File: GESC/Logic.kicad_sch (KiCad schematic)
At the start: 45 parts, among them J10 BOOT0, J11 NRST, J12 TYPE-C-31-M-12, J13 Conn_01x07, J9 STLINK, U4 STM32F405RGTx, Y1 8MHz

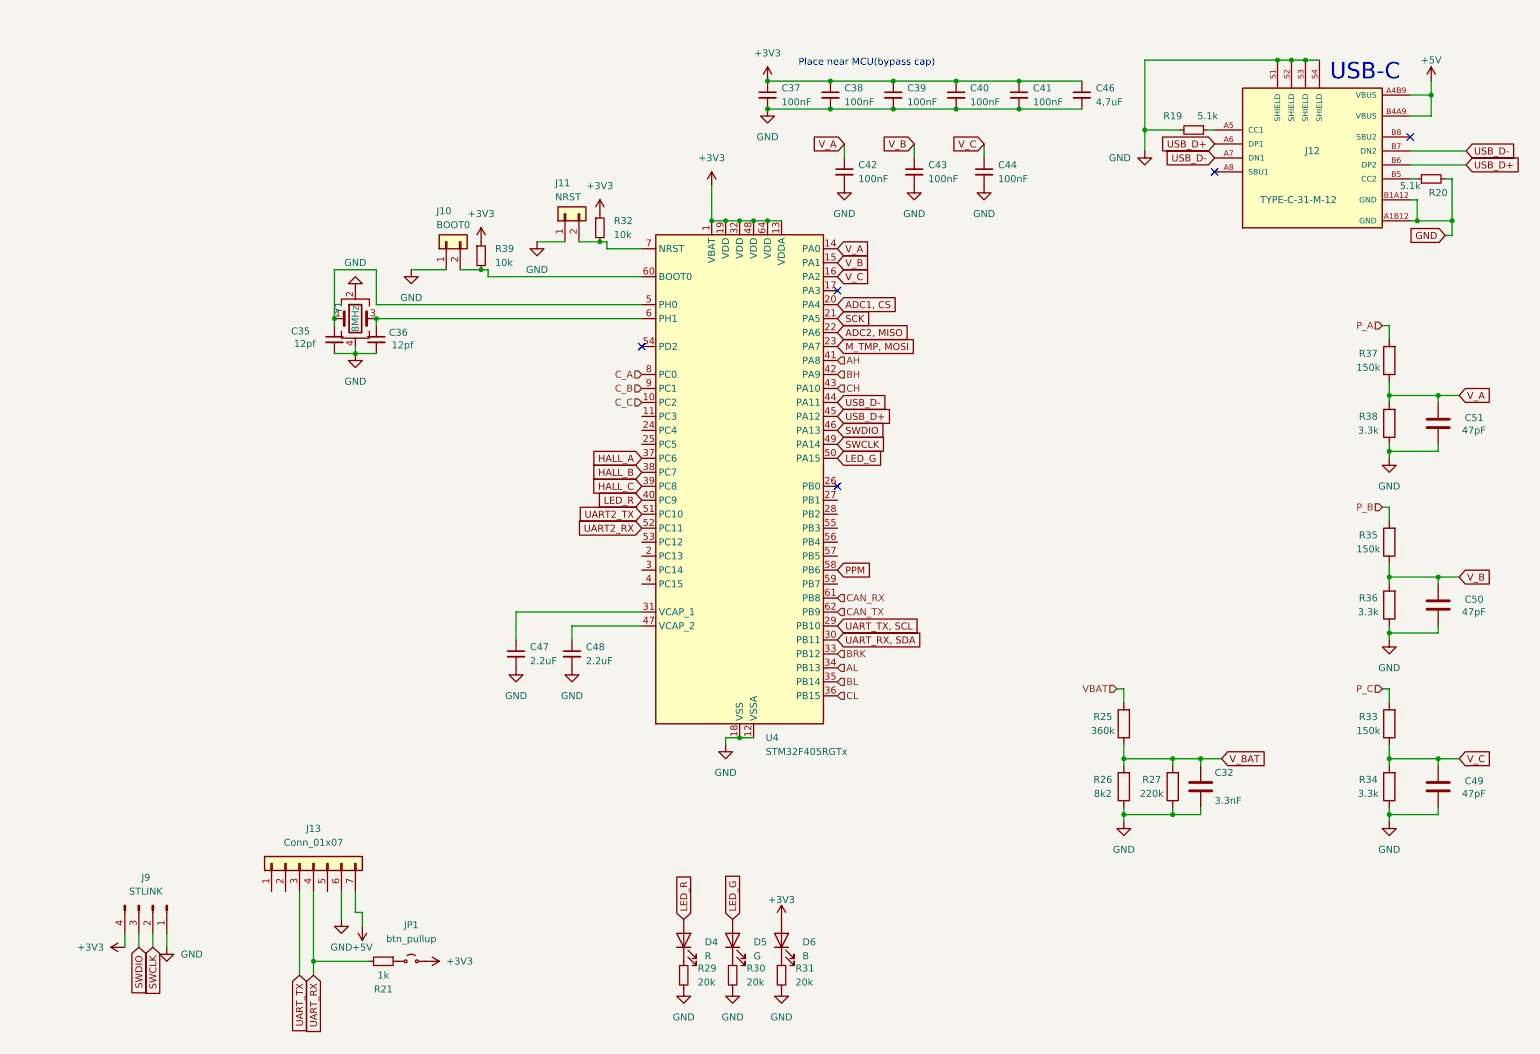
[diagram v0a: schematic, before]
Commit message: ninebot style conn
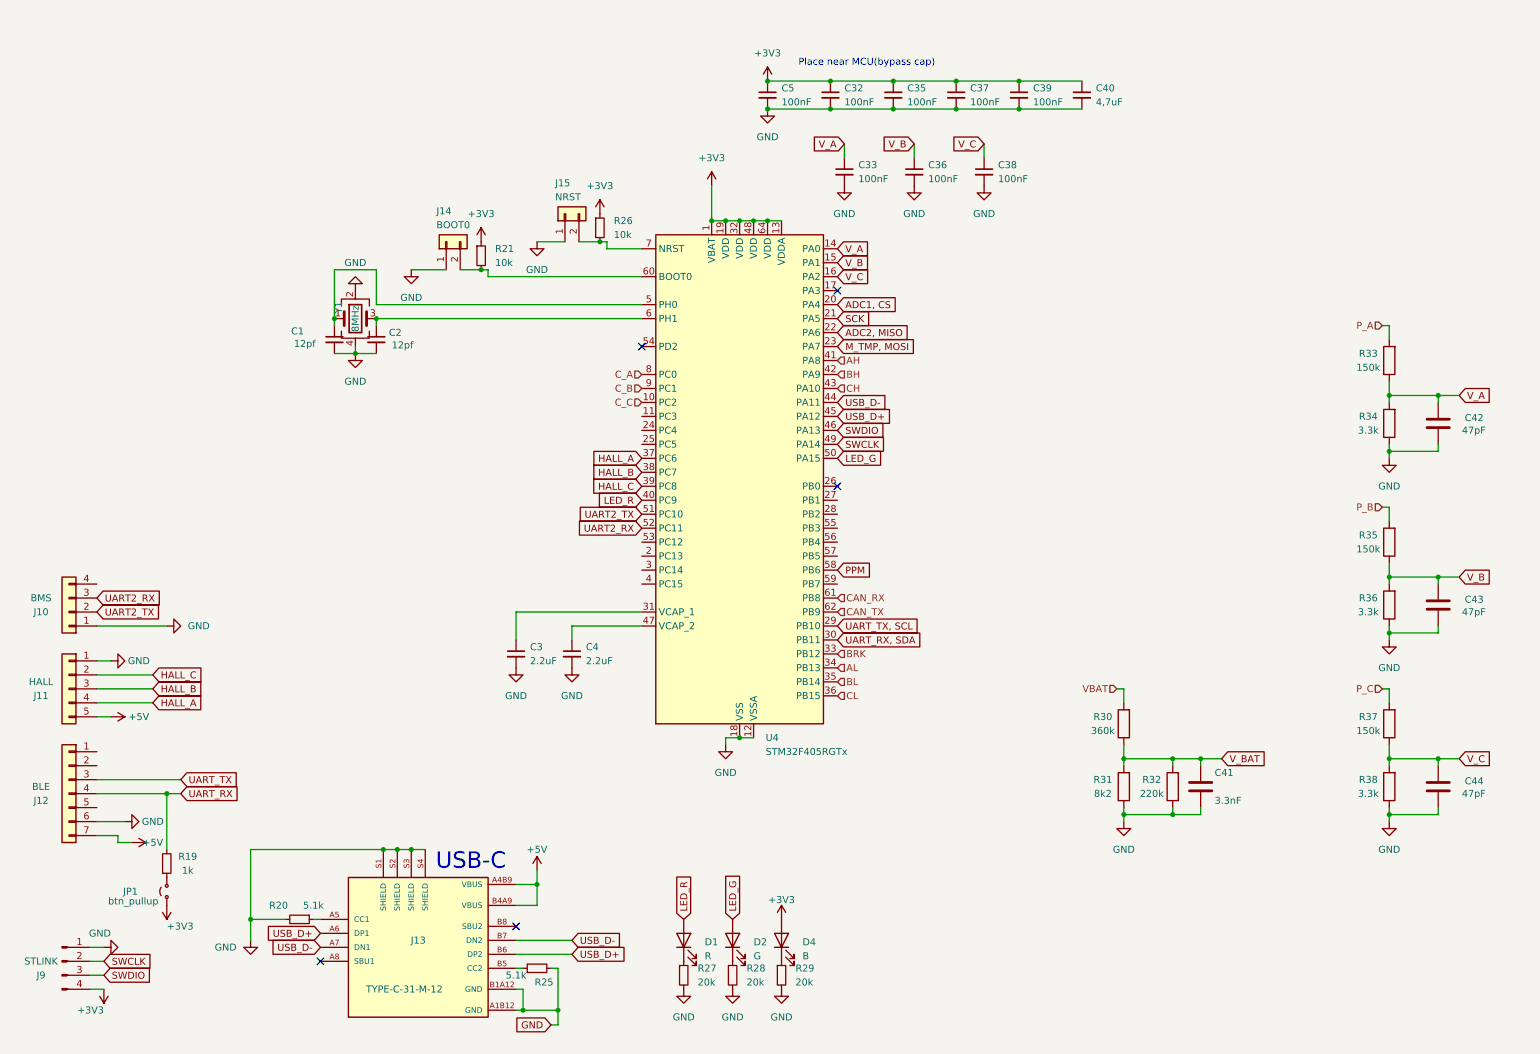
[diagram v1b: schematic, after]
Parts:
- removed C32: 3.3nF, Capacitor_SMD:C_0603_1608Metric, symbol Device:C
- removed C41, C42, C43, C44: 100nF, symbol Device:C_Small
- removed C46: 4,7uF, symbol Device:C_Small
- removed C47, C48: 2.2uF, symbol Device:C_Small
- removed C49, C50, C51: 47pF, Capacitor_SMD:C_0603_1608Metric, symbol Device:C
- removed D5: G, LED_SMD:LED_0603_1608Metric, symbol Device:LED
- removed D6: B, LED_SMD:LED_0603_1608Metric, symbol Device:LED
- removed J10: BOOT0, symbol Connector_Generic:Conn_01x02
- removed J11: NRST, symbol Connector_Generic:Conn_01x02
- removed J12: TYPE-C-31-M-12, Connector_USB:USB_C_Receptacle_HRO_TYPE-C-31-M-12, symbol TYPE-C-31-M-12:TYPE-C-31-M-12
- removed J13: Conn_01x07, symbol Connector_Generic:Conn_01x07
- removed R25: 360k, Resistor_SMD:R_0805_2012Metric, symbol Device:R
- removed R26: 8k2, Resistor_SMD:R_0603_1608Metric, symbol Device:R
- removed R27: 220k, Resistor_SMD:R_0603_1608Metric, symbol Device:R
- removed R30, R31: 20k, Resistor_SMD:R_0603_1608Metric, symbol Device:R_Small
- removed R32, R39: 10k, symbol Device:R_Small
- added C1, C2: 12pf, Capacitor_SMD:C_0603_1608Metric, symbol Device:C_Small
- added C3, C4: 2.2uF, symbol Device:C_Small
- added C32, C33, C5: 100nF, symbol Device:C_Small
- added C41: 3.3nF, Capacitor_SMD:C_0603_1608Metric, symbol Device:C
- added C42, C43, C44: 47pF, Capacitor_SMD:C_0603_1608Metric, symbol Device:C
- added D1: R, LED_SMD:LED_0603_1608Metric, symbol Device:LED
- added D2: G, LED_SMD:LED_0603_1608Metric, symbol Device:LED
- added J10: BMS, symbol Connector_Generic:Conn_01x04
- added J11: HALL, symbol Connector_Generic:Conn_01x05
- added J12: BLE, symbol Connector_Generic:Conn_01x07
- added J13: TYPE-C-31-M-12, Connector_USB:USB_C_Receptacle_HRO_TYPE-C-31-M-12, symbol TYPE-C-31-M-12:TYPE-C-31-M-12
- added J14: BOOT0, symbol Connector_Generic:Conn_01x02
- added J15: NRST, symbol Connector_Generic:Conn_01x02
- added R25: 5.1k, Resistor_SMD:R_0402_1005Metric, symbol Device:R_Small
- added R26: 10k, symbol Device:R_Small
- added R27, R28: 20k, Resistor_SMD:R_0603_1608Metric, symbol Device:R_Small
- added R30: 360k, Resistor_SMD:R_0805_2012Metric, symbol Device:R
- added R31: 8k2, Resistor_SMD:R_0603_1608Metric, symbol Device:R
- added R32: 220k, Resistor_SMD:R_0603_1608Metric, symbol Device:R
- C35, C36: value 12pf -> 100nF; footprint Capacitor_SMD:C_0603_1608Metric -> (none); LCSC C519482 -> (none)
- C40: value 100nF -> 4,7uF
- D4: value R -> B; LCSC C2286 -> C2689219
- R19: value 5.1k -> 1k; footprint Resistor_SMD:R_0402_1005Metric -> (none); LCSC C105872 -> (none)
- R21: value 1k -> 10k
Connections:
- net +3V3: now also C35.1, D4.2 (A), R21.1, C32.1, C5.1, R26.1; no longer C38.1
- net +5V: now also J11.5 (Pin_5), J12.7 (Pin_7), J13.A4B9 (VBUS), J13.B4A9 (VBUS)
- net GND: now also C1.2, C2.2, C3.2, C32.2, C33.2, C4.2, C41.2, C42.2, C43.2, C44.2, C5.2, J10.1 (Pin_1), J11.1 (Pin_1), J12.6 (Pin_6), J13.A1B12 (GND), J13.B1A12 (GND), J13.S1 (SHIELD), J13.S2 (SHIELD), J13.S3 (SHIELD), J13.S4 (SHIELD), J14.1 (Pin_1), J15.1 (Pin_1), R25.2, R27.2, R28.2, R31.1, R32.1; no longer R19.2
- net HALL_A: now also J11.4 (Pin_4)
- net HALL_B: now also J11.3 (Pin_3)
- net HALL_C: now also J11.2 (Pin_2)
- net LED_G: now also D2.2 (A)
- net LED_R: now also D1.2 (A); no longer D4.2 (A)
- net P_A: now also R33.2; no longer R37.2
- net P_C: now also R37.2; no longer R33.2
- net UART2_RX: now also J10.3 (Pin_3)
- net UART2_TX: now also J10.2 (Pin_2)
- net UART_RX: now also R19.2, J12.4 (Pin_4); no longer R21.2
- net UART_TX: now also J12.3 (Pin_3)
- net USB_D+: now also J13.A6 (DP1), J13.B6 (DP2)
- net USB_D-: now also J13.A7 (DN1), J13.B7 (DN2)
- net VBAT: now also R30.2
- net V_A: now also R33.1, R34.2, C33.1, C42.1; no longer R37.1, R38.2
- net V_B: now also C36.1, C43.1
- net V_BAT: now also C41.1, R30.1, R31.2, R32.2
- net V_C: now also C38.1, R37.1, R38.2, C44.1; no longer R33.1, R34.2
- net at U4.60 (BOOT0): now also R21.2, J14.2 (Pin_2)
- net at R19.1: now also JP1.1 (A)
- net at U4.7 (NRST): now also J15.2 (Pin_2), R26.2
- net at U4.31 (VCAP_1): now also C3.1
- net at U4.5 (PH0), Y1.1: now also C1.1; no longer C35.1
- net at U4.6 (PH1), Y1.3: now also C2.1; no longer C36.1
- net at U4.47 (VCAP_2): now also C4.1
- net at R20.1: now also J13.A5 (CC1)
- new net: D2.1 (K), R28.1
- new net: D1.1 (K), R27.1
- new net: J13.B5 (CC2), R25.1

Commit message: full to power board only
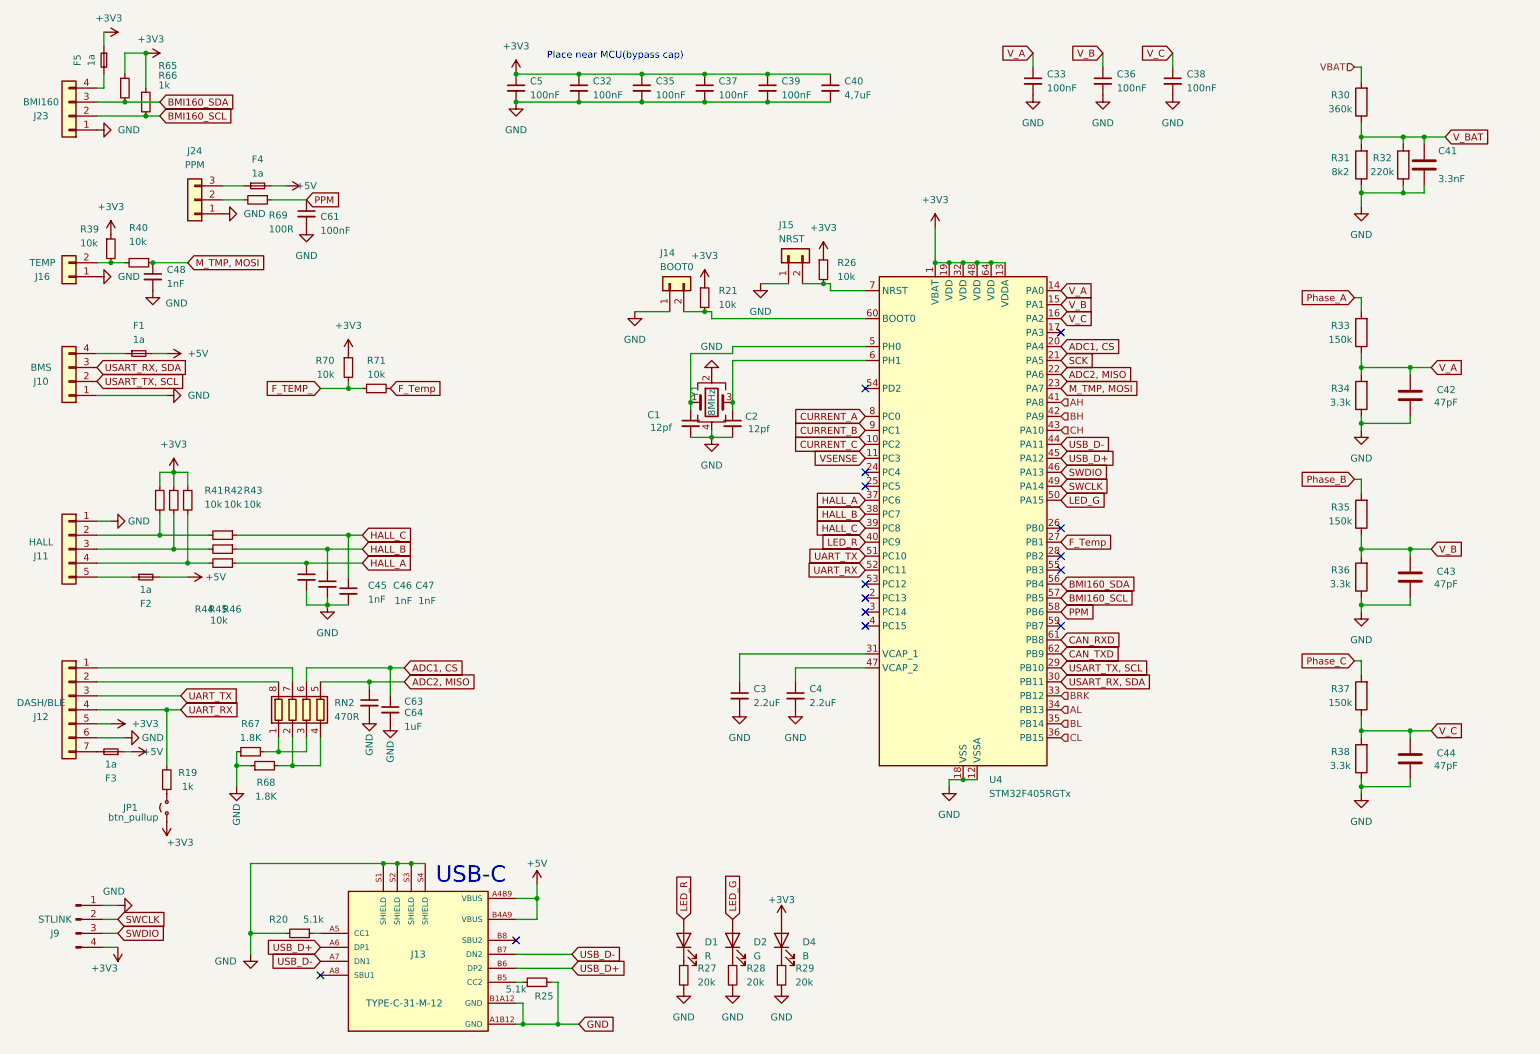
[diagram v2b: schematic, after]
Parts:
- added C45, C46, C47, C48: 1nF, Capacitor_SMD:C_0603_1608Metric, symbol Device:C_Small
- added C61: 100nF, Capacitor_SMD:C_0603_1608Metric, symbol Device:C_Small
- added C63, C64: 1uF, Capacitor_SMD:C_0402_1005Metric, symbol Device:C_Small
- added F1, F2, F3, F4, F5: 1a, Resistor_SMD:R_1206_3216Metric, symbol Device:Fuse_Small
- added J16: TEMP, Connector_JST:JST_GH_BM02B-GHS-TBT_1x02-1MP_P1.25mm_Vertical, symbol Connector_Generic:Conn_01x02
- added J23: BMI160, Connector_JST:JST_GH_BM04B-GHS-TBT_1x04-1MP_P1.25mm_Vertical, symbol Connector_Generic:Conn_01x04
- added J24: PPM, Connector_JST:JST_GH_BM03B-GHS-TBT_1x03-1MP_P1.25mm_Vertical, symbol Connector_Generic:Conn_01x03
- added R39, R40, R41, R42, R43, R65, R70, R71: 10k, Resistor_SMD:R_0603_1608Metric, symbol Device:R_Small
- added R44, R45, R46: 10k, Resistor_SMD:R_0402_1005Metric, symbol Device:R_Small
- added R66: 1k, Resistor_SMD:R_0603_1608Metric, symbol Device:R_Small
- added R67, R68: 1.8K, Resistor_SMD:R_0603_1608Metric, symbol Device:R_Small
- added R69: 100R, Resistor_SMD:R_0603_1608Metric, symbol Device:R_Small
- added RN2: 470R, Resistor_SMD:R_Array_Convex_4x0603, symbol Device:R_Pack04
- C3, C32, C33, C35, C36, C37, C38, C39, C4, C40, C5: footprint (none) -> Capacitor_SMD:C_0603_1608Metric
- J10: footprint (none) -> Connector_JST:JST_GH_BM04B-GHS-TBT_1x04-1MP_P1.25mm_Vertical
- J11: footprint (none) -> Connector_JST:JST_GH_BM05B-GHS-TBT_1x05-1MP_P1.25mm_Vertical
- J12: value BLE -> DASH/BLE; footprint (none) -> Connector_JST:JST_GH_BM07B-GHS-TBT_1x07-1MP_P1.25mm_Vertical
- J14, J15: footprint (none) -> Connector_PinSocket_2.54mm:PinSocket_1x02_P2.54mm_Vertical
- JP1: footprint (none) -> Jumper:SolderJumper-2_P1.3mm_Open_RoundedPad1.0x1.5mm
- R19, R21, R26: footprint (none) -> Resistor_SMD:R_0603_1608Metric
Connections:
- net UART_RX, SDA is gone; now on net USART_RX, SDA: U4.30 (PB11)
- net UART_TX, SCL is gone; now on net USART_TX, SCL: U4.29 (PB10)
- net +3V3: now also J12.5 (Pin_5), F5.1, R39.1, R41.1, R42.1, R43.1, R65.1, R66.1, R70.1
- net +5V: now also F1.2, F2.2, F3.1, F4.2; no longer J11.5 (Pin_5), J12.7 (Pin_7)
- net ADC1, CS: now also C64.1, RN2.6 (R3.2)
- net ADC2, MISO: now also C63.1, RN2.5 (R4.2)
- net GND: now also C45.2, C46.2, C47.2, C48.2, C61.2, C63.2, C64.2, J16.1 (Pin_1), J23.1 (Pin_1), J24.1 (Pin_1), R67.1, R68.1
- net HALL_A: now also C45.1, R46.1; no longer J11.4 (Pin_4)
- net HALL_B: now also C46.1, R45.1; no longer J11.3 (Pin_3)
- net HALL_C: now also C47.1, R44.1; no longer J11.2 (Pin_2)
- net M_TMP, MOSI: now also C48.1, R40.1
- net PPM: now also C61.1, R69.1
- net UART_RX: now also U4.52 (PC11)
- net UART_TX: now also U4.51 (PC10)
- net at J12.1 (Pin_1): now also RN2.7 (R2.2)
- net at J12.2 (Pin_2): now also RN2.8 (R1.2)
- net VSENSE: now reaches U4.11 (PC3)
- net F_Temp: now reaches U4.27 (PB1)
- net F_Temp: now also R71.2
- net BMI160_SDA: now reaches U4.56 (PB4)
- net BMI160_SDA: now also J23.3 (Pin_3), R65.2
- net BMI160_SCL: now reaches U4.57 (PB5)
- net BMI160_SCL: now also J23.2 (Pin_2), R66.2
- net at J10.4 (Pin_4): now also F1.1
- net CAN_RX renamed CAN_RXD
- net CAN_TX renamed CAN_TXD
- net C_A renamed CURRENT_A
- net C_B renamed CURRENT_B
- net C_C renamed CURRENT_C
- net P_A renamed Phase_A
- net P_B renamed Phase_B
- net P_C renamed Phase_C
- net UART2_RX renamed USART_RX, SDA
- net USART_RX, SDA: no longer U4.52 (PC11)
- net UART2_TX renamed USART_TX, SCL
- net USART_TX, SCL: no longer U4.51 (PC10)
- new net: F3.2, J12.7 (Pin_7)
- new net: J11.4 (Pin_4), R43.2, R46.2
- new net: J16.2 (Pin_2), R39.2, R40.2
- new net: J24.2 (Pin_2), R69.2
- new net: F4.1, J24.3 (Pin_3)
- new net: J11.3 (Pin_3), R42.2, R45.2
- new net: R67.2, RN2.1 (R1.1), RN2.3 (R3.1)
- new net: J11.2 (Pin_2), R41.2, R44.2
- new net: F2.1, J11.5 (Pin_5)
- new net: F5.2, J23.4 (Pin_4)
- new net: R68.2, RN2.2 (R2.1), RN2.4 (R4.1)
- new net F_TEMP_: R70.2, R71.1
- no-connect marks 5 -> 14
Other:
- moved on the sheet: C1, C2, C3, C32, C33, C35, C36, C37, C38, C39, C4, C40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
